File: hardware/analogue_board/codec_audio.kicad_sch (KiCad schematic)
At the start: 63 parts, among them J303 Codec RST, J310 Holes, left top, J311 Holes, left bottom, J312 Holes, right top, J313 Holes, right middle, U301 PCM3060PWR, U302 TL074HIDR

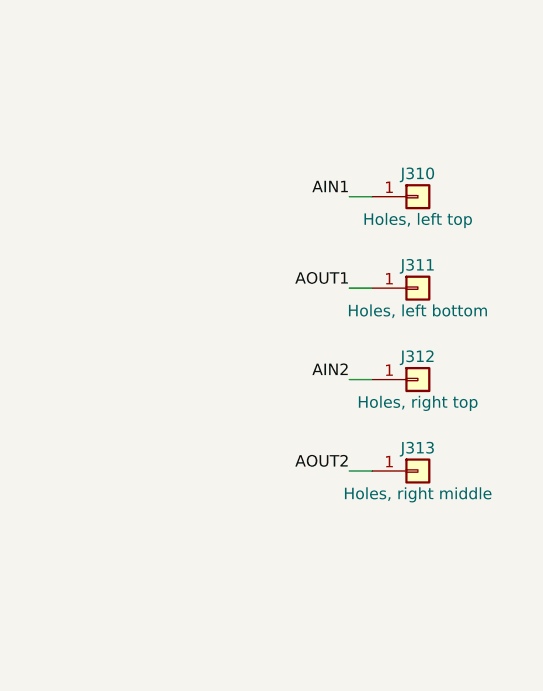
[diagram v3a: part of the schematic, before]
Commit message: Analogue board: bus chips level with their module pins; design rules; trial autoroute
Re-floorplan the centre channel in the order of the module's buses (SPI-A,
SPI-B, I2S, I2C), so the codec is 6 mm from the Pico's I2S pins instead of
38 mm; CV output op-amps move to the top-right corner.

Net classes (0.15/0.15 default, 0.3 power) and an In1 ground plane are
written into the project. autoroute.py runs Freerouting on a copy of the
board to measure routability. Schematic hole groups no longer overlap.

Co-Authored-By: Claude Opus 5.5 <noreply@anthropic.com>
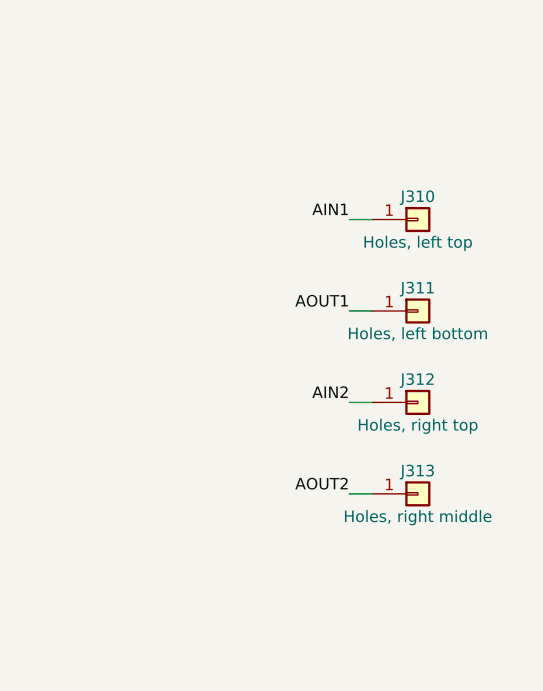
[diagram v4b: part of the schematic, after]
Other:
- moved on the sheet: J310, J311, J312, J313
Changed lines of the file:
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@@
 	(symbol
 		(lib_id "Connector_Generic:Conn_01x01")
-		(at 340.36 60.96 0)
+		(at 340.36 63.5 0)
 		(unit 1)
 		(exclude_from_sim no)
@@
 		(dnp no)
 		(property "Reference" "J310"
-			(at 340.36 58.42 0)
+			(at 340.36 60.96 0)
 			(effects
 				(font (size 1.27 1.27))
@@
 		)
 		(property "Value" "Holes, left top"
+			(at 340.36 66.04 0)
+			(effects
+				(font (size 1.27 1.27))
+			)
+		)
+		(property "Footprint" "analogue_board:WiringHoles_1x01"
 			(at 340.36 63.5 0)
 			(effects
 				(font (size 1.27 1.27))
-			)
-		)
-		(property "Footprint" "analogue_board:WiringHoles_1x01"
-			(at 340.36 60.96 0)
-			(effects
-				(font (size 1.27 1.27))
 				(hide yes)
 			)
 		)
 		(property "Datasheet" ""
-			(at 340.36 60.96 0)
+			(at 340.36 63.5 0)
 			(effects
 				(font (size 1.27 1.27))
@@
 		)
 		(property "Description" ""
-			(at 340.36 60.96 0)
+			(at 340.36 63.5 0)
 			(effects
 				(font (size 1.27 1.27))
@@
 		)
 		(property "JLC" "bare holes"
-			(at 340.36 60.96 0)
+			(at 340.36 63.5 0)
 			(effects
 				(font (size 1.27 1.27))
@@
 	)
 	(label "AIN1"
-		(at 332.74 60.96 180)
+		(at 332.74 63.5 180)
 		(effects
 			(font (size 1.27 1.27))
@@
 	(symbol
 		(lib_id "Connector_Generic:Conn_01x01")
-		(at 340.36 71.12 0)
+		(at 340.36 73.66 0)
 		(unit 1)
 		(exclude_from_sim no)
@@
 		(dnp no)
 		(property "Reference" "J311"
-			(at 340.36 68.58 0)
+			(at 340.36 71.12 0)
 			(effects
 				(font (size 1.27 1.27))
@@
 		)
 		(property "Value" "Holes, left bottom"
+			(at 340.36 76.2 0)
+			(effects
+				(font (size 1.27 1.27))
+			)
+		)
+		(property "Footprint" "analogue_board:WiringHoles_1x01"
 			(at 340.36 73.66 0)
 			(effects
 				(font (size 1.27 1.27))
-			)
-		)
-		(property "Footprint" "analogue_board:WiringHoles_1x01"
-			(at 340.36 71.12 0)
-			(effects
-				(font (size 1.27 1.27))
 				(hide yes)
 			)
 		)
 		(property "Datasheet" ""
-			(at 340.36 71.12 0)
+			(at 340.36 73.66 0)
 			(effects
 				(font (size 1.27 1.27))
@@
 		)
 		(property "Description" ""
-			(at 340.36 71.12 0)
+			(at 340.36 73.66 0)
 			(effects
 				(font (size 1.27 1.27))
@@
 		)
 		(property "JLC" "bare holes"
-			(at 340.36 71.12 0)
+			(at 340.36 73.66 0)
 			(effects
 				(font (size 1.27 1.27))
@@
 	)
 	(label "AOUT1"
-		(at 332.74 71.12 180)
+		(at 332.74 73.66 180)
 		(effects
 			(font (size 1.27 1.27))
@@
 	(symbol
 		(lib_id "Connector_Generic:Conn_01x01")
-		(at 340.36 81.28 0)
+		(at 340.36 83.82 0)
 		(unit 1)
 		(exclude_from_sim no)
@@
 		(dnp no)
 		(property "Reference" "J312"
-			(at 340.36 78.74 0)
+			(at 340.36 81.28 0)
 			(effects
 				(font (size 1.27 1.27))
@@
 		)
 		(property "Value" "Holes, right top"
+			(at 340.36 86.36 0)
+			(effects
+				(font (size 1.27 1.27))
+			)
+		)
+		(property "Footprint" "analogue_board:WiringHoles_1x01"
 			(at 340.36 83.82 0)
 			(effects
 				(font (size 1.27 1.27))
-			)
-		)
-		(property "Footprint" "analogue_board:WiringHoles_1x01"
-			(at 340.36 81.28 0)
-			(effects
-				(font (size 1.27 1.27))
 				(hide yes)
 			)
 		)
 		(property "Datasheet" ""
-			(at 340.36 81.28 0)
+			(at 340.36 83.82 0)
 			(effects
 				(font (size 1.27 1.27))
@@
 		)
 		(property "Description" ""
-			(at 340.36 81.28 0)
+			(at 340.36 83.82 0)
 			(effects
 				(font (size 1.27 1.27))
@@
 		)
 		(property "JLC" "bare holes"
-			(at 340.36 81.28 0)
+			(at 340.36 83.82 0)
 			(effects
 				(font (size 1.27 1.27))
@@
 	)
 	(label "AIN2"
-		(at 332.74 81.28 180)
+		(at 332.74 83.82 180)
 		(effects
 			(font (size 1.27 1.27))
@@
 	(symbol
 		(lib_id "Connector_Generic:Conn_01x01")
-		(at 340.36 91.44 0)
+		(at 340.36 93.98 0)
 		(unit 1)
 		(exclude_from_sim no)
@@
 		(dnp no)
 		(property "Reference" "J313"
-			(at 340.36 88.9 0)
+			(at 340.36 91.44 0)
 			(effects
 				(font (size 1.27 1.27))
@@
 		)
 		(property "Value" "Holes, right middle"
+			(at 340.36 96.52 0)
+			(effects
+				(font (size 1.27 1.27))
+			)
+		)
+		(property "Footprint" "analogue_board:WiringHoles_1x01"
 			(at 340.36 93.98 0)
 			(effects
 				(font (size 1.27 1.27))
-			)
-		)
-		(property "Footprint" "analogue_board:WiringHoles_1x01"
-			(at 340.36 91.44 0)
-			(effects
-				(font (size 1.27 1.27))
 				(hide yes)
 			)
 		)
 		(property "Datasheet" ""
-			(at 340.36 91.44 0)
+			(at 340.36 93.98 0)
 			(effects
 				(font (size 1.27 1.27))
@@
 		)
 		(property "Description" ""
-			(at 340.36 91.44 0)
+			(at 340.36 93.98 0)
 			(effects
 				(font (size 1.27 1.27))
@@
 		)
 		(property "JLC" "bare holes"
-			(at 340.36 91.44 0)
+			(at 340.36 93.98 0)
 			(effects
 				(font (size 1.27 1.27))
@@
 	)
 	(label "AOUT2"
-		(at 332.74 91.44 180)
+		(at 332.74 93.98 180)
 		(effects
 			(font (size 1.27 1.27))
@@
 	)
 	(wire
-		(pts (xy 332.74 60.96) (xy 335.28 60.96))
-		(stroke (width 0) (type default))
-	)
-	(wire
-		(pts (xy 332.74 71.12) (xy 335.28 71.12))
-		(stroke (width 0) (type default))
-	)
-	(wire
-		(pts (xy 332.74 81.28) (xy 335.28 81.28))
-		(stroke (width 0) (type default))
-	)
-	(wire
-		(pts (xy 332.74 91.44) (xy 335.28 91.44))
-		(stroke (width 0) (type default))
-	)
+		(pts (xy 332.74 63.5) (xy 335.28 63.5))
+		(stroke (width 0) (type default))
+	)
+	(wire
+		(pts (xy 332.74 73.66) (xy 335.28 73.66))
+		(stroke (width 0) (type default))
+	)
+	(wire
+		(pts (xy 332.74 83.82) (xy 335.28 83.82))
+		(stroke (width 0) (type default))
+	)
+	(wire
+		(pts (xy 332.74 93.98) (xy 335.28 93.98))
+		(stroke (width 0) (type default))
+	)
